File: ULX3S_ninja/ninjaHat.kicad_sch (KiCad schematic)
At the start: 2 parts, among them J1 DVI-HX-107DIP, P1 ULX3S connector (JP1)

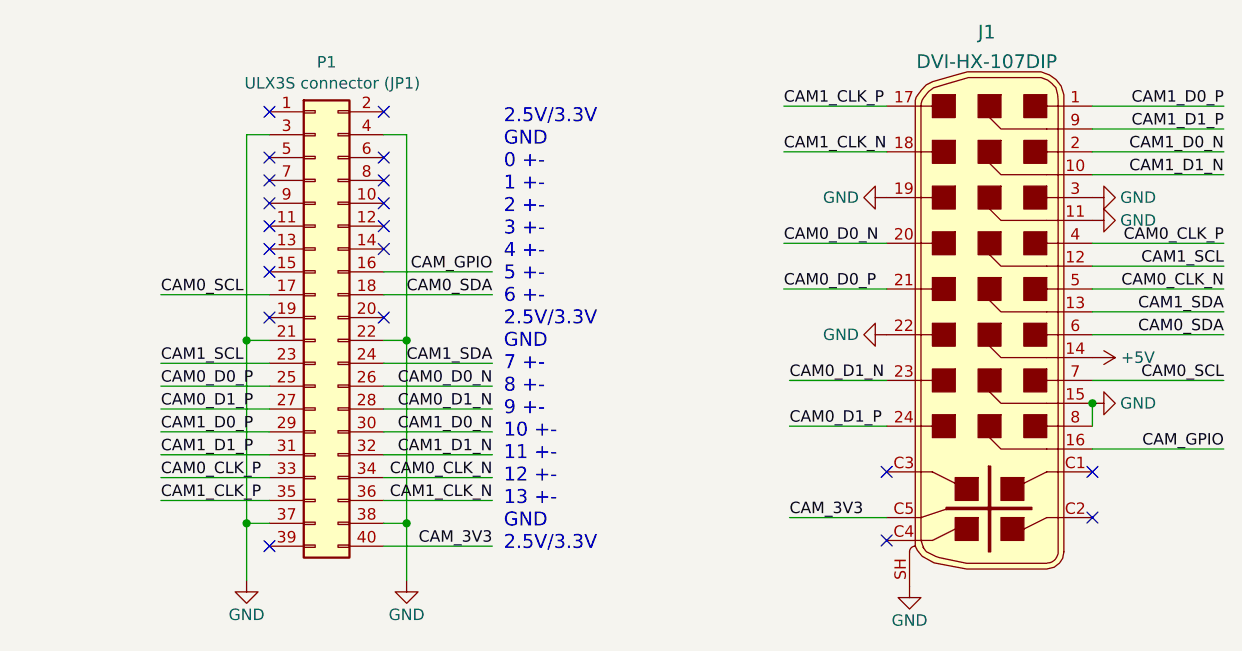
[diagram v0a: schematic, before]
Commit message: new Revision for FPGA Ninja
Termination Resistors and 4 Impus per lane and clk
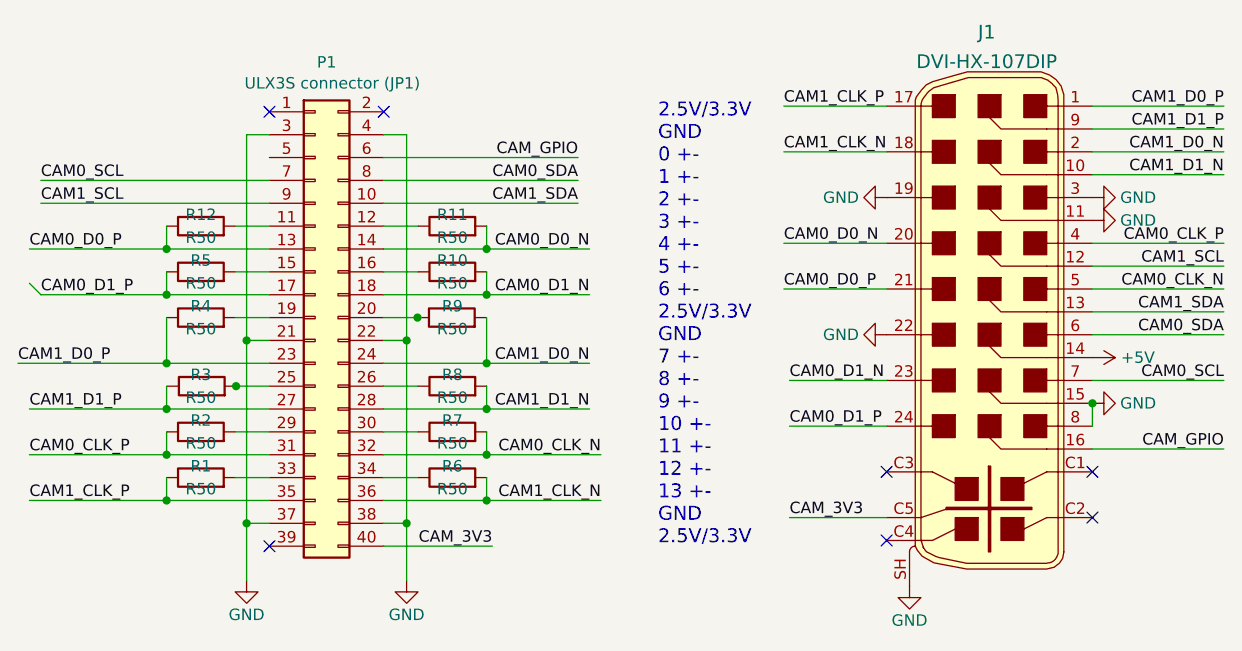
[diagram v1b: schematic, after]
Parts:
- added R1, R10, R11, R12, R2, R3, R4, R5, R6, R7, R8, R9: R50, symbol Device:R
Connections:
- net CAM0_CLK_N: now also P1.32 (Pin_32), R7.2; no longer P1.34 (Pin_34)
- net CAM0_CLK_P: now also P1.31 (Pin_31), R2.1; no longer P1.33 (Pin_33)
- net CAM0_D0_N: now also P1.14 (Pin_14), R11.2; no longer P1.26 (Pin_26)
- net CAM0_D0_P: now also P1.13 (Pin_13), R12.1; no longer P1.25 (Pin_25)
- net CAM0_D1_N: now also P1.18 (Pin_18), R10.2; no longer P1.28 (Pin_28)
- net CAM0_D1_P: now also P1.17 (Pin_17), R5.1; no longer P1.27 (Pin_27)
- net CAM0_SCL: now also P1.7 (Pin_7); no longer P1.17 (Pin_17)
- net CAM0_SDA: now also P1.8 (Pin_8); no longer P1.18 (Pin_18)
- net CAM1_CLK_N: now also R6.2
- net CAM1_CLK_P: now also R1.1
- net CAM1_D0_N: now also P1.24 (Pin_24); no longer P1.30 (Pin_30)
- net CAM1_D0_P: now also P1.23 (Pin_23), R4.1; no longer P1.29 (Pin_29)
- net CAM1_D1_N: now also P1.28 (Pin_28), R8.2; no longer P1.32 (Pin_32)
- net CAM1_D1_P: now also P1.27 (Pin_27); no longer P1.31 (Pin_31)
- net CAM1_SCL: now also P1.9 (Pin_9); no longer P1.23 (Pin_23)
- net CAM1_SDA: now also P1.10 (Pin_10); no longer P1.24 (Pin_24)
- net CAM_GPIO: now also P1.6 (Pin_6); no longer P1.16 (Pin_16)
- net at P1.11 (Pin_11): now also R12.2
- net at P1.12 (Pin_12): now also R11.1
- net at P1.15 (Pin_15): now also R5.2
- net at P1.19 (Pin_19): now also R4.2
- net at P1.20 (Pin_20): now also R9.1
- new net: P1.16 (Pin_16), R10.1
- new net: P1.25 (Pin_25), R3.2
- new net: P1.26 (Pin_26), R8.1
- new net: P1.29 (Pin_29), R2.2
- new net: P1.30 (Pin_30), R7.1
- new net: P1.33 (Pin_33), R1.2
- new net: P1.34 (Pin_34), R6.1
- no-connect marks 20 -> 7

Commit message: Changed circuit
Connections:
- net CAM0_D0_N: now also P1.12 (Pin_12); no longer P1.14 (Pin_14)
- net CAM0_D0_P: now also P1.11 (Pin_11); no longer P1.13 (Pin_13)
- net CAM0_D1_N: now also P1.16 (Pin_16); no longer P1.18 (Pin_18)
- net CAM0_D1_P: now also P1.15 (Pin_15); no longer P1.17 (Pin_17)
- net CAM0_SCL: now also P1.5 (Pin_5); no longer P1.7 (Pin_7)
- net CAM0_SDA: now also P1.6 (Pin_6); no longer P1.8 (Pin_8)
- net CAM1_D0_N: now also R9.2
- net CAM1_D1_P: now also R3.1
- net CAM1_SCL: now also P1.7 (Pin_7); no longer P1.9 (Pin_9)
- net CAM1_SDA: now also P1.8 (Pin_8); no longer P1.10 (Pin_10)
- net CAM_GPIO: now also P1.2 (Pin_2); no longer P1.6 (Pin_6)
- net at R12.2: now also P1.9 (Pin_9); no longer P1.11 (Pin_11)
- net at R11.1: now also P1.10 (Pin_10); no longer P1.12 (Pin_12)
- net at R5.2: now also P1.13 (Pin_13); no longer P1.15 (Pin_15)
- net at R10.1: now also P1.14 (Pin_14); no longer P1.16 (Pin_16)
- net at R4.2: now also P1.17 (Pin_17); no longer P1.19 (Pin_19)
- net at R9.1: now also P1.18 (Pin_18); no longer P1.20 (Pin_20)
- no-connect marks 7 -> 6
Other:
- moved on the sheet: R10, R11, R12, R4, R5, R9
